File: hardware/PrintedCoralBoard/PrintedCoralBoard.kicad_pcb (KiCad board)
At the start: 4 copper layers, 90.2 x 95.9 mm, 14 parts, among them J1 DF40HC_3.0_-100DS-0.4V_51_, J2 DF40HC_3.0_-100DS-0.4V_51_, J4 Conn_02x25_Odd_Even, J5 Conn_02x25_Odd_Even, J6 Conn_02x25_Odd_Even, J7 Conn_02x25_Odd_Even

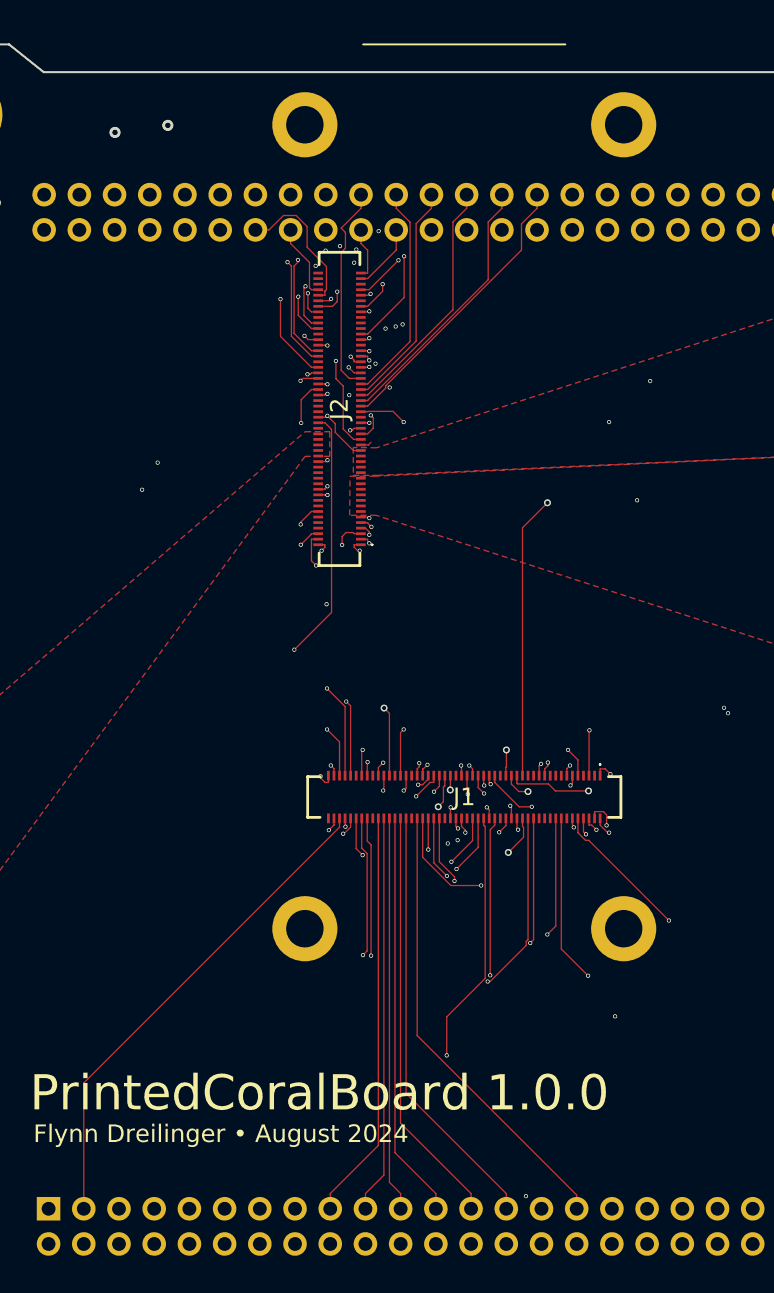
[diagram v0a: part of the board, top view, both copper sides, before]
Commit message: fix landing pattern
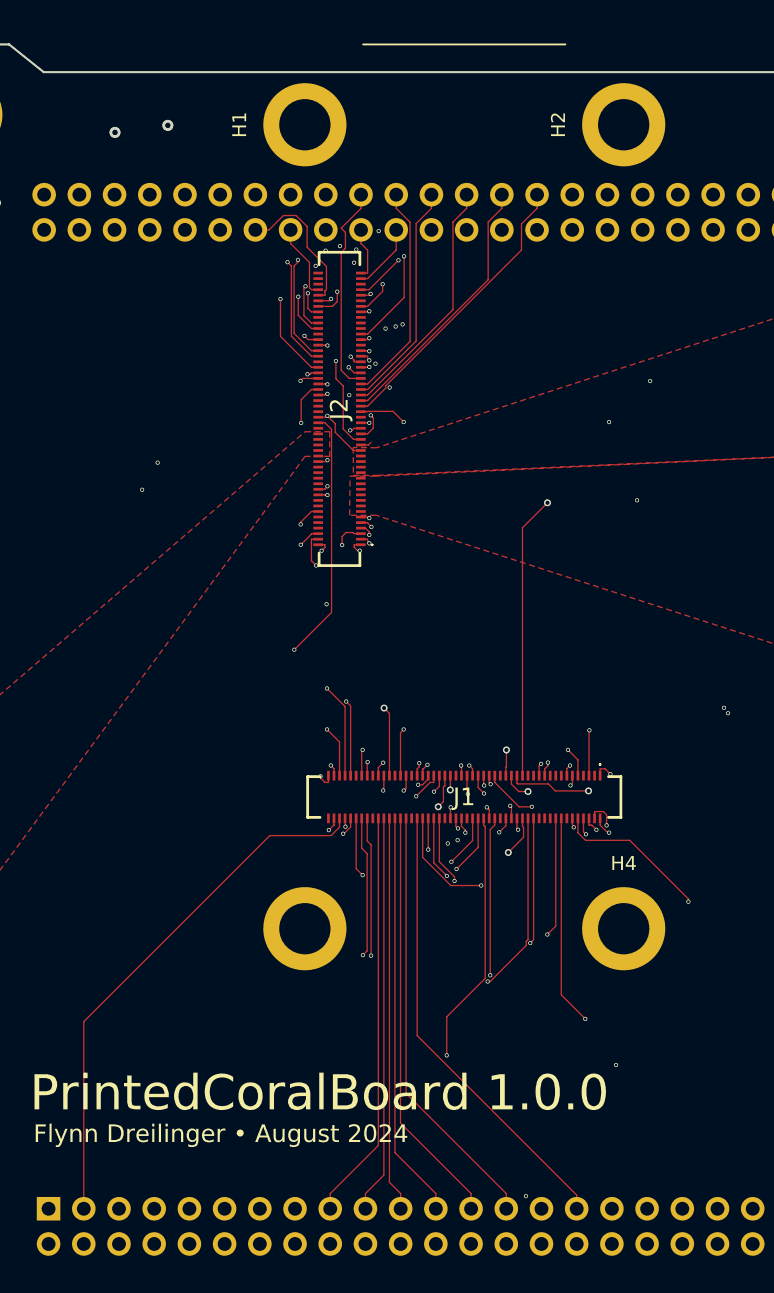
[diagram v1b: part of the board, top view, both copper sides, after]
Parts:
- H1, H2, H3, H4: footprint MountingHole:MountingHole_2.7mm_M2.5_DIN965_Pad -> adcs:CoralLandingPad
- moved H3 23.0 mm to (33.5, 63.8), turned to 0 degrees
- moved H4 23.0 mm to (56.5, 63.8), turned to 0 degrees
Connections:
- J7 pad 15: unconnected-(J7-Pin_15-Pad15) -> GND
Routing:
- net LPUART1_RXD: track 34.1 -> 36.9 mm
- net WL_REG_ON: track 35.0 -> 37.7 mm
- net DAC_OUT: track 35.8 -> 38.4 mm
- net MIC_CLK: track 36.7 -> 39.2 mm
- net I2C1_SCL: track 40.7 -> 43.2 mm
- net LPSPI6_SCK: track 50.7 -> 53.0 mm
- net I2C1_SDA: track 53.4 -> 55.6 mm
- net FLEXPWM1_PWM1_A: track 34.0 -> 36.2 mm
- net SAI2_TX_DATA: track 39.2 -> 41.4 mm
- net FLEXPWM2_PWM1_B: track 38.5 -> 40.5 mm
- net FLEXPWM1_PWM1_B: track 36.8 -> 38.7 mm
- net FLEXPWM1_PWM0_B: track 35.9 -> 37.7 mm
- net FLEXPWM1_PWM0_A: track 35.0 -> 36.8 mm
- net FLEXPWM2_PWM1_A: track 39.0 -> 40.7 mm
- net LPUART6_RTS: track 45.4 -> 46.4 mm
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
